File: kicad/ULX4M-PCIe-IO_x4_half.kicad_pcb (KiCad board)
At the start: 4 copper layers, 167.7 x 111.2 mm, 32 parts, among them J1 PCIexpress_bracket, J10 FCR684205R, J2 PCIexpress_x4, J3 SFP+, J4 SFP+, J5 Conn_02x20_Odd_Even, J6 Conn_02x05_Odd_Even, J7 Micro_SD_Card_CD, J8 Conn_02x05_Odd_Even, J9 FCR684205T, P1 HDMI-D, SW1 SW_DIP_x08, SW2 SW_DIP_x08

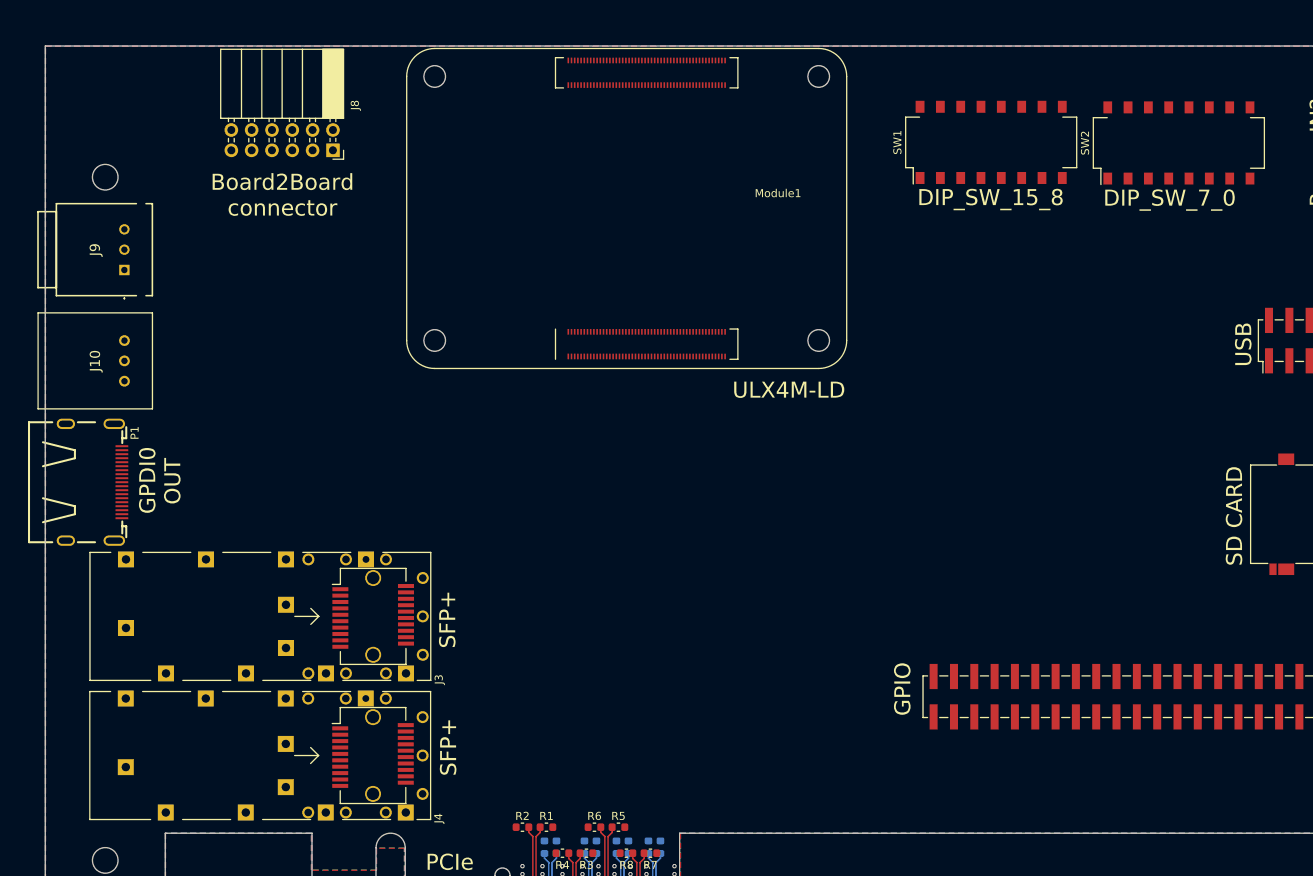
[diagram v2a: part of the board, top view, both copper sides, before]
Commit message: Adding picture and reference boards
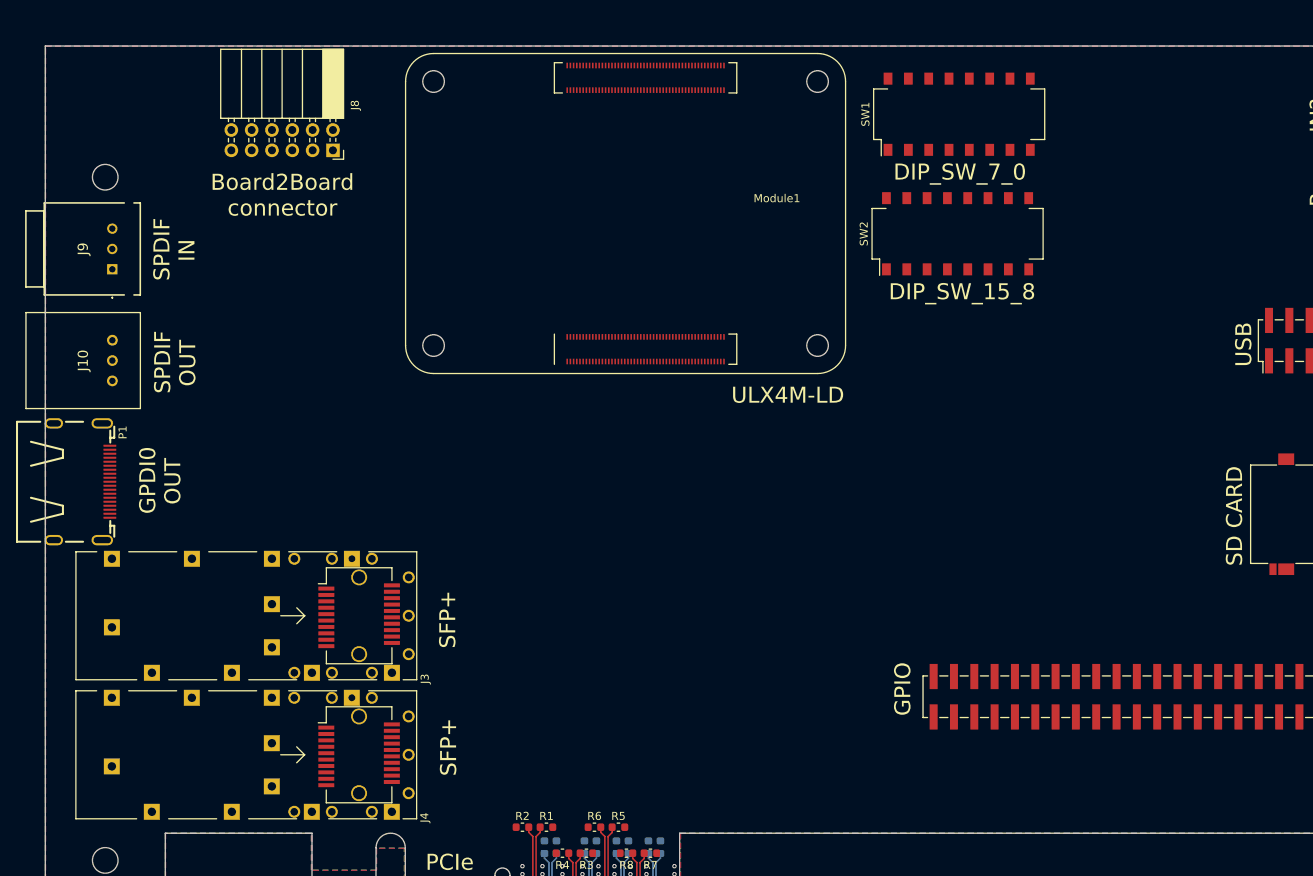
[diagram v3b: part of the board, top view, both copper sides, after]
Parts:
- moved SW2 29.9 mm to (178.5, 106.4)
- moved SW1 5.33 mm to (178.7, 91.5)
- moved J3 1.76 mm to (109.9, 154.2)
- moved J4 1.75 mm to (109.9, 171.6)
- moved J9 1.51 mm to (72.9, 110.9)
- moved J10 1.51 mm to (72.9, 119.8)
- moved P1 1.50 mm to (67.0, 137.4)
- moved Module1 0.65 mm to (161.0, 120.4)
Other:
- board text added: "IN"
- board text added: "SPDIF"
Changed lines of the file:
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@@
         (effects (font (size 2 2) (thickness 0.25)))
     )
-    (fp_text user "Full height max" (at 36.75 -108.25) (layer "Cmts.User")
+    (fp_text user "Full height max" (at 48.62 0.94) (layer "Cmts.User")
         (effects (font (size 2 2) (thickness 0.25)))
     )
@@
         (effects (font (size 1 1) (thickness 0.15)))
     )
-    (fp_text user "Low profile max height" (at 39.25 -71) (layer "Cmts.User")
+    (fp_text user "Low profile max height" (at 54.06 -2.22) (layer "Cmts.User")
         (effects (font (size 2 2) (thickness 0.25)))
     )
-    (fp_text user "Max component height: solder side 2,67mm component side 14,49mm" (at 40 -44.25) (layer "Cmts.User")
+    (fp_text user "Max component height: solder side 2,67mm component side 14,49mm" (at 89.74 -5.69) (layer "Cmts.User")
         (effects (font (size 2 2) (thickness 0.25)))
     )
@@
   )
   (footprint "Button_Switch_SMD:SW_DIP_SPSTx08_Slide_Omron_A6S-810x_W8.9mm_P2.54mm" (layer "F.Cu")
-    (at 182.715 95.025 90)
+    (at 178.715 91.505 90)
     (descr "SMD 8x-dip-switch SPST Omron_A6S-810x, Slide, row spacing 8.9 mm (350 mils), body size  (see http://omronfs.omron.com/en_US/ecb/products/pdf/en-a6s.pdf)")
     (tags "SMD DIP Switch SPST Slide 8.9mm 350mil")
@@
     (pad "16" smd rect (at 4.45 -8.89 90) (size 1.5 1.1) (layers "F.Cu" "F.Paste" "F.Mask")
       (net 397 "unconnected-(SW1-Pad16)") (pintype "passive"))
-    (model "${KISYS3DMOD}/Button_Switch_SMD.3dshapes/SW_DIP_SPSTx08_Slide_Omron_A6S-810x_W8.9mm_P2.54mm.wrl"
+    (model ":KICAD6_3DMODEL_DIR:Button_Switch_SMD.3dshapes/SW_DIP_SPSTx08_Slide_Omron_A6S-810x_W8.9mm_P2.54mm.wrl"
       (offset (xyz 0 0 0))
       (scale (xyz 1 1 1))
@@
   )
   (footprint "Button_Switch_SMD:SW_DIP_SPSTx08_Slide_Omron_A6S-810x_W8.9mm_P2.54mm" (layer "F.Cu")
-    (at 206.175 95.095 90)
+    (at 178.515 106.445 90)
     (descr "SMD 8x-dip-switch SPST Omron_A6S-810x, Slide, row spacing 8.9 mm (350 mils), body size  (see http://omronfs.omron.com/en_US/ecb/products/pdf/en-a6s.pdf)")
     (tags "SMD DIP Switch SPST Slide 8.9mm 350mil")
@@
       (rotate (xyz 0 0 0))
     )
+    (model ":KICAD6_3DMODEL_DIR:Button_Switch_SMD.3dshapes/SW_DIP_SPSTx08_Slide_Omron_A6S-810x_W8.9mm_P2.54mm.wrl"
+      (offset (xyz 0 0 0))
+      (scale (xyz 1 1 1))
+      (rotate (xyz 0 0 0))
+    )
   )
   (footprint "Connector_Coaxial:SMA_Amphenol_132289_EdgeMount" (layer "F.Cu")
@@
       (rotate (xyz 0 0 0))
     )
+    (model ":KICAD6_3DMODEL_DIR:Connector_PinSocket_2.54mm.3dshapes/PinSocket_2x06_P2.54mm_Horizontal.wrl"
+      (offset (xyz 0 0 0))
+      (scale (xyz 1 1 1))
+      (rotate (xyz 0 0 0))
+    )
   )
   (footprint "Connector:Connector_SFP_and_Cage" (layer "F.Cu")
-    (at 111.665 154.275)
+    (at 109.91 154.195)
     (descr "https://www.te.com/commerce/DocumentDelivery/DDEController?Action=srchrtrv&DocNm=2227302&DocType=Customer+Drawing&DocLang=English")
     (tags "SFP+ SFP")
@@
   )
   (footprint "Connector:Connector_SFP_and_Cage" (layer "F.Cu")
-    (at 111.645 171.665)
+    (at 109.9 171.575)
     (descr "https://www.te.com/commerce/DocumentDelivery/DDEController?Action=srchrtrv&DocNm=2227302&DocType=Customer+Drawing&DocLang=English")
     (tags "SFP+ SFP")
@@
       (rotate (xyz 0 0 0))
     )
+    (model ":KICAD6_3DMODEL_DIR:Connector_PinHeader_2.54mm.3dshapes/PinHeader_2x20_P2.54mm_Vertical_SMD.wrl"
+      (offset (xyz 0 0 0))
+      (scale (xyz 1 1 1))
+      (rotate (xyz 0 0 0))
+    )
   )
   (footprint "Connector_PinHeader_2.54mm:PinHeader_2x05_P2.54mm_Vertical_SMD" (layer "F.Cu")
@@
       (rotate (xyz 0 0 0))
     )
+    (model ":KICAD6_3DMODEL_DIR:Connector_PinHeader_2.54mm.3dshapes/PinHeader_2x05_P2.54mm_Vertical_SMD.step"
+      (offset (xyz 0 0 0))
+      (scale (xyz 1 1 1))
+      (rotate (xyz 0 0 0))
+    )
   )
   (footprint "micro-sd:SCHD3A100" (layer "F.Cu")
@@
   )
   (footprint "FCR684205-R:FCR684205R" (layer "F.Cu")
-    (at 74.375 119.795 -90)
+    (at 72.865 119.755 -90)
     (descr "ORJ-5_2")
     (tags "Undefined or Miscellaneous")
@@
     (pad "3" thru_hole circle (at 5.08 0 270) (size 1.35 1.35) (drill 0.8) (layers *.Cu *.Mask)
       (net 381 "unconnected-(J10-VCC)") (pinfunction "VCC") (pintype "passive"))
-    (model "FCR684205R.stp"
-      (offset (xyz 0 0 0))
+    (model "D:/projects/nlnet/ULX4M-PCIe-IO/Library/FCR684205-R/Cliff_-_FCR684205R.step"
+      (offset (xyz 2.5 -4 0))
       (scale (xyz 1 1 1))
       (rotate (xyz 0 0 0))
@@
   )
   (footprint "CM4IO:Raspberry-Pi-4-Compute-Module" (layer "F.Cu")
-    (at 161.155 119.785 90)
+    (at 161.015 120.415 90)
     (descr "Raspberry Pi 4 Compute Module")
     (tags "Raspberry Pi 4 Compute Module")
@@
     (pad "200" smd rect (at 35 -11.7) (size 0.2 0.7) (layers "F.Cu" "F.Paste" "F.Mask")
       (net 355 "unconnected-(Module1B-HDMI0_SCL)") (pinfunction "HDMI0_SCL") (pintype "open_collector"))
-    (model "./CM4.3dshapes/DF40C-100DS.stp"
-      (offset (xyz -0.46 15.38 0))
-      (scale (xyz 1 1 1))
-      (rotate (xyz -90 0 0))
-    )
-    (model "./CM4IO.3dshapes/DF40C-100DS.stp"
-      (offset (xyz 33.46 15.38 0))
-      (scale (xyz 1 1 1))
-      (rotate (xyz -90 0 0))
+    (model "${KIPRJMOD}/libraries/3D/ulx4m-ld.wrl"
+      (offset (xyz 110.5 147.5 2))
+      (scale (xyz 0.4 0.4 0.4))
+      (rotate (xyz 0 0 90))
     )
   )
   (footprint "FCR684205-T:FCR684205T" (layer "F.Cu")
-    (at 74.365 110.975 -90)
+    (at 72.855 110.885 -90)
     (descr "FCR684205T-2")
     (tags "Connector")
@@
     (pad "3" thru_hole circle (at -5.08 0 270) (size 1.3 1.3) (drill 0.8) (layers *.Cu *.Mask)
       (net 378 "unconnected-(J9-VIN)") (pinfunction "VIN") (pintype "passive"))
-    (model "FCR684205T.stp"
-      (offset (xyz 0 0 0))
+    (model "D:/projects/nlnet/ULX4M-PCIe-IO/Library/FCR684205-T/Cliff_-_FCR684205T.step"
+      (offset (xyz -2.5 -3.5 0))
       (scale (xyz 1 1 1))
       (rotate (xyz 0 0 0))
@@
   )
   (footprint "hdmi-d:HDMI-D" (layer "F.Cu")
-    (at 68.50245 137.505 180)
+    (at 67.00245 137.445 180)
     (descr "PADOVETE OT 1.6X0.28 STAVAT NA 1.6X0.25")
     (tags "PADOVETE OT 1.6X0.28 STAVAT NA 1.6X0.25")
@@
     (pad "19" smd rect (at -5.55 4.5 180) (size 1.6 0.25) (layers "F.Cu" "F.Paste" "F.Mask")
       (net 357 "unconnected-(P1-P19)") (pinfunction "P19") (pintype "passive") (solder_mask_margin 0.05) (solder_paste_margin -0.01))
+    (model "${KIPRJMOD}/libraries/hdmi-d/hdmi-d.3dshapes/10029449-111RLF.wrl"
+      (offset (xyz -3 0 3.5))
+      (scale (xyz 0.4 0.4 0.4))
+      (rotate (xyz 180 0 -90))
+    )
   )
   (footprint "Capacitor_SMD:C_0603_1608Metric" (layer "B.Cu")
@@
   (gr_line (start 109.475 183.2) (end 109.475 193.625)
     (stroke (width 0.15) (type solid)) (layer "Edge.Cuts"))
-  (gr_text "DIP_SW_7_0" (at 205.025 102.005) (layer "F.SilkS")
+  (gr_text "DIP_SW_7_0" (at 178.805 98.745) (layer "F.SilkS")
     (effects (font (size 2 2) (thickness 0.4)))
   )
@@
     (effects (font (size 2 2) (thickness 0.4)))
   )
-  (gr_text "ULX4M-LD" (at 157.435 126.005) (layer "F.SilkS")
+  (gr_text "ULX4M-LD" (at 157.295 126.635) (layer "F.SilkS")
     (effects (font (size 2 2) (thickness 0.4)))
   )
@@
     (effects (font (size 2 2) (thickness 0.4)))
   )
-  (gr_text "DIP_SW_15_8" (at 182.655 101.935) (layer "F.SilkS")
+  (gr_text "DIP_SW_15_8" (at 179.085 113.705) (layer "F.SilkS")
     (effects (font (size 2 2) (thickness 0.4)))
   )
@@
     (effects (font (size 2 2) (thickness 0.4)))
   )
+  (gr_text "SPDIF" (at 79.165 122.495 90) (layer "F.SilkS")
+    (effects (font (size 2 2) (thickness 0.4)))
+  )
+  (gr_text "IN" (at 82.195 108.525 90) (layer "F.SilkS")
+    (effects (font (size 2 2) (thickness 0.4)))
+  )
+  (gr_text "SPDIF" (at 79.065 108.395 90) (layer "F.SilkS")
+    (effects (font (size 2 2) (thickness 0.4)))
+  )
   (gr_text "USB" (at 214.295 120.285 90) (layer "F.SilkS")
     (effects (font (size 2 2) (thickness 0.4)))
   )
+  (gr_text "OUT" (at 82.295 122.625 90) (layer "F.SilkS")
+    (effects (font (size 2 2) (thickness 0.4)))
+  )

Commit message: Adding PCIe power connector - fix 31
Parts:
- added J11: OLED, Connector_PinHeader_2.54mm:PinHeader_1x08_P2.54mm_Vertical, F.Cu at (134.2, 131.4)
- added J12: 641737-1, 641737-1:641737-1, F.Cu at (215.1, 95.7)
- added J13: 39-30-0060, 39-30-0060:39-30-Y060, F.Cu at (221.1, 115.9)
- added REF**: OSHW-Logo2_14.6x12mm_SilkScreen, Symbol:OSHW-Logo2_14.6x12mm_SilkScreen, F.Cu at (201.7, 92.1)
- added REF**: KiCad-Logo2_6mm_SilkScreen, Symbol:KiCad-Logo2_6mm_SilkScreen, F.Cu at (184.8, 159.0)
- added U1: TPD4E02B04DQA, Package_SON:USON-10_2.5x1.0mm_P0.5mm, F.Cu at (125.5, 172.6)
- added U10: TPD4E02B04DQA, Package_SON:USON-10_2.5x1.0mm_P0.5mm, F.Cu at (116.2, 160.5)
- added U11: TPD4E02B04DQA, Package_SON:USON-10_2.5x1.0mm_P0.5mm, F.Cu at (116.1, 166.9)
- added U12: TPD4E02B04DQA, Package_SON:USON-10_2.5x1.0mm_P0.5mm, F.Cu at (116.1, 173.2)
- added U13: AT24CS32-SSHM, Package_SO:SOIC-8_3.9x4.9mm_P1.27mm, F.Cu at (200.4, 158.4)
- added U2: TPD4E02B04DQA, Package_SON:USON-10_2.5x1.0mm_P0.5mm, F.Cu at (128.4, 172.6)
- added U3: TPD4E02B04DQA, Package_SON:USON-10_2.5x1.0mm_P0.5mm, F.Cu at (131.3, 172.6)
- added U4: TPD4E02B04DQA, Package_SON:USON-10_2.5x1.0mm_P0.5mm, F.Cu at (134.1, 172.6)
- added U5: TPD4E02B04DQA, Package_SON:USON-10_2.5x1.0mm_P0.5mm, F.Cu at (137.0, 172.6)
- added U6: TPD4E02B04DQA, Package_SON:USON-10_2.5x1.0mm_P0.5mm, F.Cu at (139.9, 172.6)
- added U7: TPD4E02B04DQA, Package_SON:USON-10_2.5x1.0mm_P0.5mm, F.Cu at (142.8, 172.6)
- added U8: TPD4E02B04DQA, Package_SON:USON-10_2.5x1.0mm_P0.5mm, F.Cu at (145.6, 172.6)
- added U9: TPD4E02B04DQA, Package_SON:USON-10_2.5x1.0mm_P0.5mm, F.Cu at (116.0, 154.2)
- moved AE2 141.9 mm to (327.6, 37.6), turned to 0 degrees
- moved AE1 122.3 mm to (345.2, 48.9), turned to 0 degrees
- moved J6 80.9 mm to (159.2, 170.2)
- moved J7 15.1 mm to (219.0, 156.1)
- moved J5 5.57 mm to (199.6, 169.9)
- moved SW2 1.69 mm to (180.2, 106.4)
- moved SW1 1.69 mm to (180.4, 91.4)
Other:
- board text added: "ID EEPROM"
- board text added: "OLED"
- board text added: "Power IN"
- board text removed: "Power IN?"

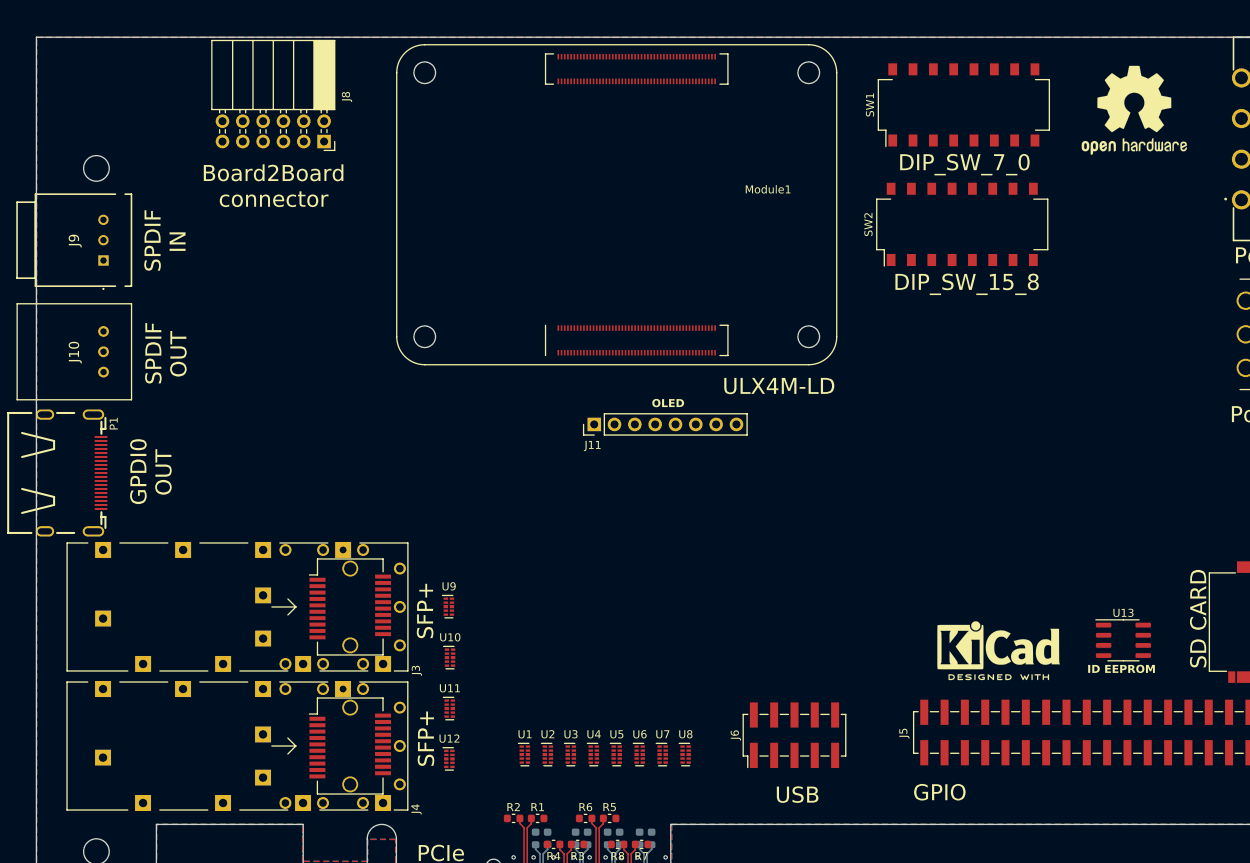
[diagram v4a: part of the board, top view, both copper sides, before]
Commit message: Adding logos and version text fix #3 fix #24
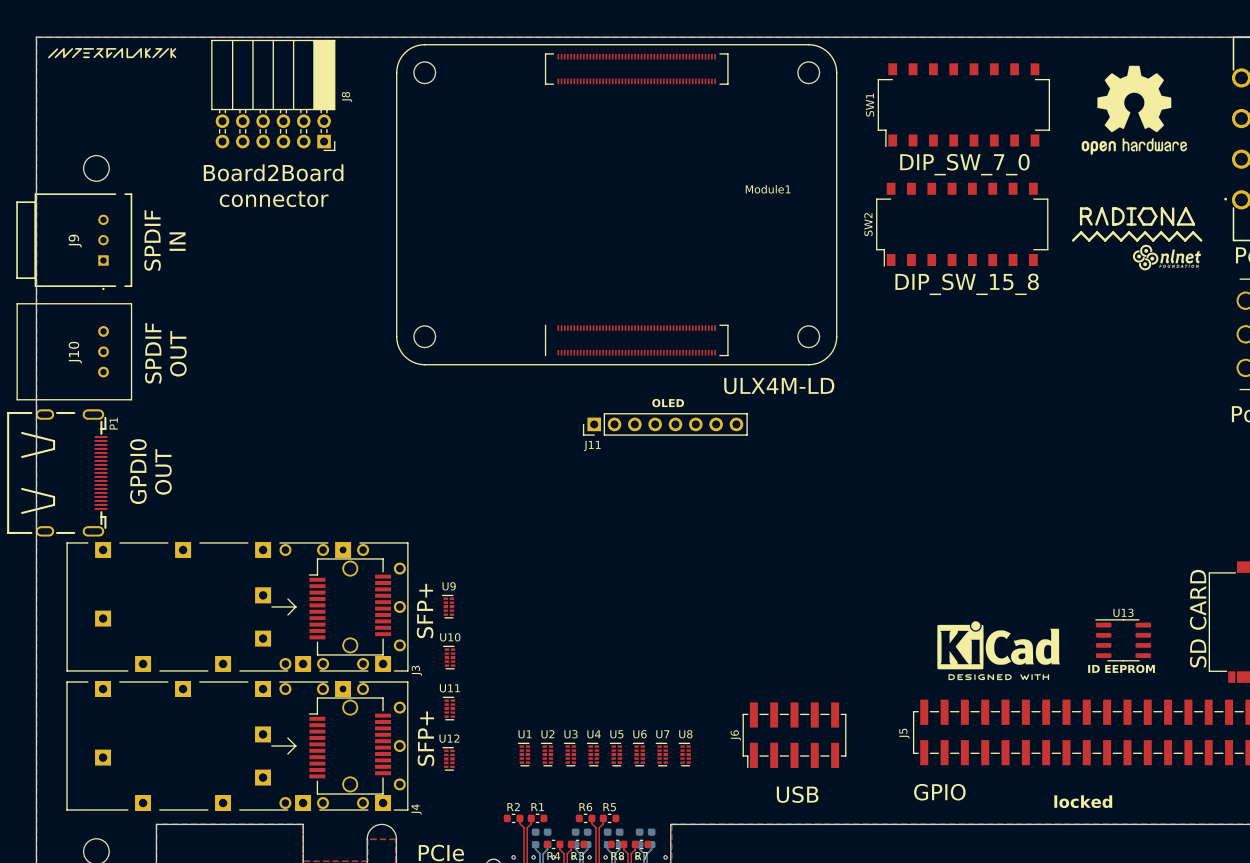
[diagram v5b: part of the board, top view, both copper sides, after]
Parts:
- added G***: LOGO, intergalaktik:intergalaktik, F.Cu at (74.0, 84.8)
- added G***: LOGO, nlnet:nlnet, F.Cu at (205.8, 110.5)
- added radiona: radiona, radiona:radiona, F.Cu at (202.1, 105.4)
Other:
- board text added: "locked"
